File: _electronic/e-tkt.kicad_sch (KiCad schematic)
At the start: 1 part

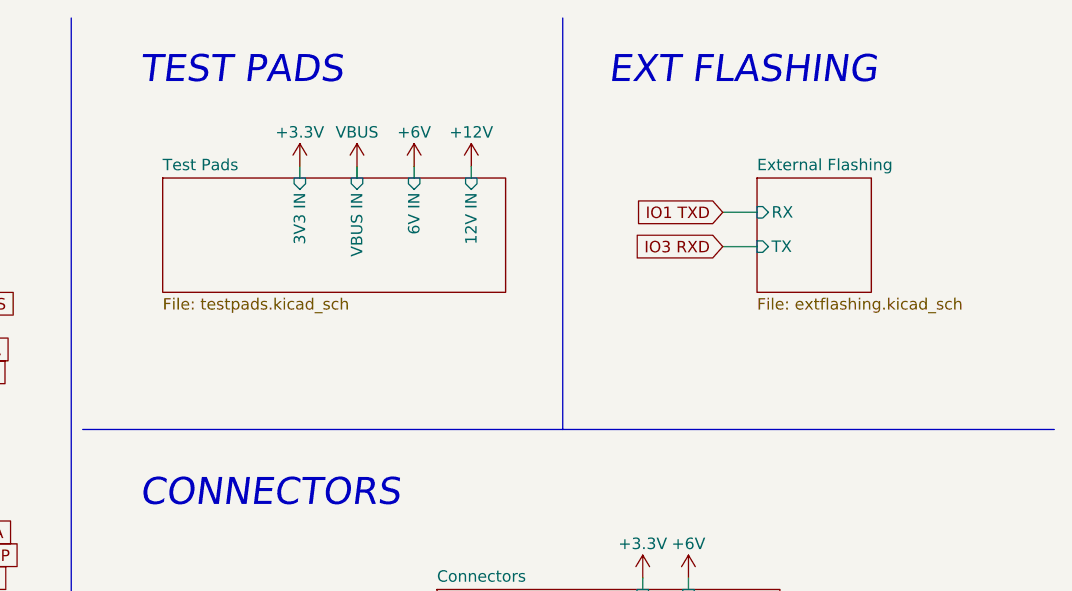
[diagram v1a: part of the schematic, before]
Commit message: revised pcb: direct power, leds, ftdi w/o 3v3
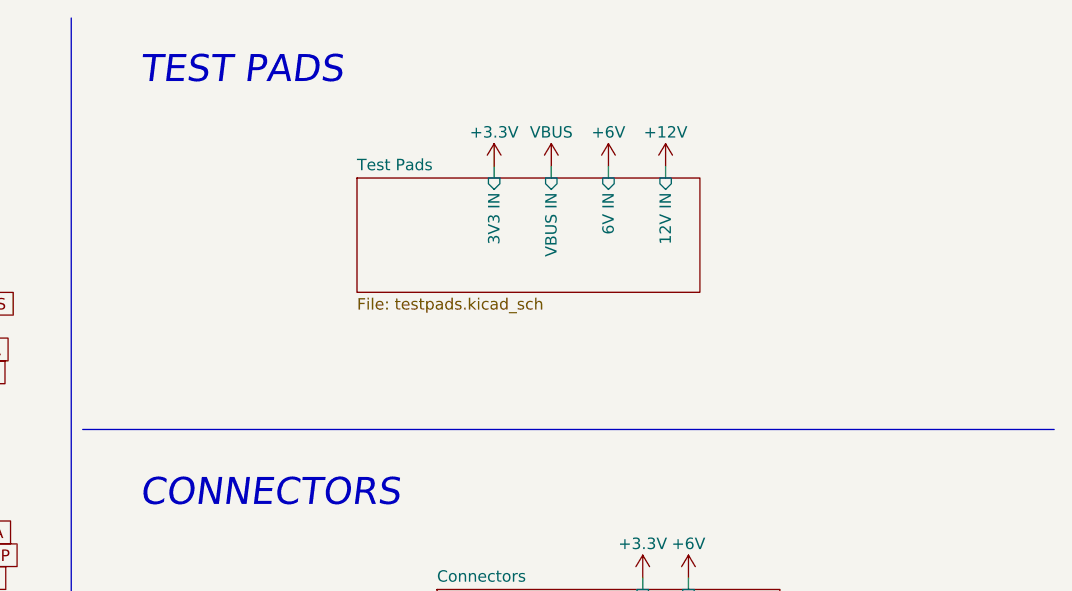
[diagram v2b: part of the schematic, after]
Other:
- removed sheet External Flashing
- note removed: "EXT FLASHING"

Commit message: v1 pcb
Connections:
- net MCU/IO27 BUZZER OUT renamed MCU/IO26 BUZZER OUT
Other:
- sheet Boot ports: added DFU OUT; removed RESET OUT
- sheet MCU ports: added IO26 BUZZER OUT; removed IO27 BUZZER OUT
- note added: "PADS"
- note removed: "TEST PADS"
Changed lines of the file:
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@@
     (stroke (width 0) (type default) (color 0 0 0 0))
   )
-  (text "TEST PADS" (at 184.15 20.32 0)
+  (text "PADS" (at 184.15 20.32 0)
     (effects (font (size 3 3) italic) (justify left bottom))
   )
@@
     )
   )
-  (global_label "IO0 RESET" (shape input) (at 67.31 109.22 0) (fields_autoplaced)
-    (effects (font (size 1.27 1.27)) (justify left))
-    (property "Intersheet References" "${INTERSHEET_REFS}" (id 0) (at 79.5807 109.1406 0)
+  (global_label "IO0 DFU" (shape input) (at 67.31 109.22 0) (fields_autoplaced)
+    (effects (font (size 1.27 1.27)) (justify left))
+    (property "Intersheet References" "${INTERSHEET_REFS}" (id 0) (at 77.5245 109.1406 0)
       (effects (font (size 1.27 1.27)) (justify left) hide)
     )
@@
     )
   )
-  (global_label "IO0 RESET" (shape input) (at 107.95 58.42 180) (fields_autoplaced)
-    (effects (font (size 1.27 1.27)) (justify right))
-    (property "Intersheet References" "${INTERSHEET_REFS}" (id 0) (at 95.6793 58.4994 0)
+  (global_label "IO0 DFU" (shape input) (at 107.95 58.42 180) (fields_autoplaced)
+    (effects (font (size 1.27 1.27)) (justify right))
+    (property "Intersheet References" "${INTERSHEET_REFS}" (id 0) (at 97.7355 58.3406 0)
       (effects (font (size 1.27 1.27)) (justify right) hide)
     )
@@
       (effects (font (size 1.27 1.27)) (justify left top))
     )
-    (pin "RESET OUT" input (at 63.5 109.22 0)
+    (pin "DFU OUT" input (at 63.5 109.22 0)
       (effects (font (size 1.27 1.27)) (justify right))
     )
@@
       (effects (font (size 1.27 1.27)) (justify right))
     )
-    (pin "IO27 BUZZER OUT" input (at 149.86 83.82 0)
+    (pin "IO26 BUZZER OUT" input (at 149.86 83.82 0)
       (effects (font (size 1.27 1.27)) (justify right))
     )
@@
       (reference "#PWR0128") (unit 1) (value "+6V") (footprint "")
     )
+    (path "/101993a2-8c13-4c99-b45a-f486b8a836ae/4741fdff-cf20-405c-8df9-b0efece63751"
+      (reference "#PWR0129") (unit 1) (value "GNDREF") (footprint "")
+    )
     (path "/101993a2-8c13-4c99-b45a-f486b8a836ae/b2ca76e4-3a79-40a6-bbdf-055e674ad637"
       (reference "#PWR0130") (unit 1) (value "GNDREF") (footprint "")
@@
       (reference "#PWR0188") (unit 1) (value "+12V") (footprint "")
     )
-    (path "/101993a2-8c13-4c99-b45a-f486b8a836ae/b900f311-a484-4187-a9ac-83ef2eca9cdf"
-      (reference "#PWR0194") (unit 1) (value "GNDREF") (footprint "")
-    )
     (path "/101993a2-8c13-4c99-b45a-f486b8a836ae/c73cd793-7bb6-49a6-8bf3-bf2dc45d0e58"
       (reference "A_NEMA1") (unit 1) (value "8+8 pin") (footprint "SnapEDA Library:Pololu_Breakout-16_15.2x20.3mm")
     )
+    (path "/53dc24b1-e06e-42b0-9cce-919318864537/c708e976-d434-4784-8384-a21eac2e20cc"
+      (reference "C_DFU1") (unit 1) (value "0.1uF 50V") (footprint "Capacitor_SMD:C_0603_1608Metric_Pad1.08x0.95mm_HandSolder")
+    )
     (path "/53dc24b1-e06e-42b0-9cce-919318864537/c161ff46-3126-42d4-ac2d-a86add82b65e"
       (reference "C_ENA1") (unit 1) (value "0.1uF 50V") (footprint "Capacitor_SMD:C_0603_1608Metric_Pad1.08x0.95mm_HandSolder")
@@
       (reference "C_POW_OUT5") (unit 1) (value "22uF 25V") (footprint "Capacitor_SMD:C_1210_3225Metric_Pad1.33x2.70mm_HandSolder")
     )
-    (path "/53dc24b1-e06e-42b0-9cce-919318864537/c708e976-d434-4784-8384-a21eac2e20cc"
-      (reference "C_RST1") (unit 1) (value "0.1uF 50V") (footprint "Capacitor_SMD:C_0603_1608Metric_Pad1.08x0.95mm_HandSolder")
-    )
     (path "/500f785f-7d37-4530-93ef-964340f250e0/29215e2e-bd3e-478f-8c8a-2609da7e48de"
       (reference "C_SER2") (unit 1) (value "47pF 5V") (footprint "Capacitor_SMD:C_0603_1608Metric_Pad1.08x0.95mm_HandSolder")
@@
       (reference "R_AUTO2") (unit 1) (value "10K (5%)") (footprint "Resistor_SMD:R_0603_1608Metric_Pad0.98x0.95mm_HandSolder")
     )
+    (path "/53dc24b1-e06e-42b0-9cce-919318864537/80289846-45bb-4f7e-8a56-6a469cee6e49"
+      (reference "R_DFU1") (unit 1) (value "10K (5%)") (footprint "Resistor_SMD:R_0603_1608Metric_Pad0.98x0.95mm_HandSolder")
+    )
     (path "/53dc24b1-e06e-42b0-9cce-919318864537/f9878306-6ebd-4529-86fc-8fe33906cf59"
       (reference "R_ENA1") (unit 1) (value "10K (5%)") (footprint "Resistor_SMD:R_0603_1608Metric_Pad0.98x0.95mm_HandSolder")
@@
       (reference "R_POW_FFB1") (unit 1) (value "11K") (footprint "Resistor_SMD:R_0603_1608Metric_Pad0.98x0.95mm_HandSolder")
     )
-    (path "/53dc24b1-e06e-42b0-9cce-919318864537/80289846-45bb-4f7e-8a56-6a469cee6e49"
-      (reference "R_RST1") (unit 1) (value "10K (5%)") (footprint "Resistor_SMD:R_0603_1608Metric_Pad0.98x0.95mm_HandSolder")
-    )
     (path "/500f785f-7d37-4530-93ef-964340f250e0/1d27ab48-a640-4f47-bc17-bdcd69db5732"
       (reference "R_RX1") (unit 1) (value "27R") (footprint "Resistor_SMD:R_0603_1608Metric_Pad0.98x0.95mm_HandSolder")
@@
       (reference "R_WIFI1") (unit 1) (value "10K(5%)") (footprint "Resistor_SMD:R_0603_1608Metric_Pad0.98x0.95mm_HandSolder")
     )
+    (path "/53dc24b1-e06e-42b0-9cce-919318864537/d348eb6c-e41c-436a-ae0e-698c5c035baa"
+      (reference "SW_DFU1") (unit 1) (value "B3FS-1000") (footprint "b3fs:B3FS-1000")
+    )
     (path "/53dc24b1-e06e-42b0-9cce-919318864537/a455153a-05f9-4e85-901e-8958d4f3b17b"
       (reference "SW_ENA1") (unit 1) (value "B3FS-1000") (footprint "b3fs:B3FS-1000")
     )
-    (path "/53dc24b1-e06e-42b0-9cce-919318864537/d348eb6c-e41c-436a-ae0e-698c5c035baa"
-      (reference "SW_RST1") (unit 1) (value "B3FS-1000") (footprint "b3fs:B3FS-1000")
-    )
     (path "/2d0c1513-867c-4f44-88ad-09ecf55e026a/29887617-5bc0-4b32-ac51-e4008f4b493b"
       (reference "SW_WIFI1") (unit 1) (value "B3FS-1000") (footprint "b3fs:B3FS-1000")
     )
-    (path "/80181399-56c9-4858-bcd2-be6de4dbffde/a2ae1716-c872-45b0-ada9-012773e72e0e"
-      (reference "TP_3.3v1") (unit 1) (value "TestPoint") (footprint "TestPoint:TestPoint_Pad_D1.0mm")
-    )
-    (path "/80181399-56c9-4858-bcd2-be6de4dbffde/7dfcde2e-43b0-42d7-8f37-7932f448318d"
-      (reference "TP_5v1") (unit 1) (value "TestPoint") (footprint "TestPoint:TestPoint_Pad_D1.0mm")
-    )
-    (path "/80181399-56c9-4858-bcd2-be6de4dbffde/0d1cefda-0da1-419e-8d72-b6b1e29406d4"
-      (reference "TP_6v1") (unit 1) (value "TestPoint") (footprint "TestPoint:TestPoint_Pad_D1.0mm")
-    )
-    (path "/80181399-56c9-4858-bcd2-be6de4dbffde/8cef06b1-cb55-4287-a2c1-e0e76cd67f80"
-      (reference "TP_12v1") (unit 1) (value "TestPoint") (footprint "TestPoint:TestPoint_Pad_D1.0mm")
-    )
-    (path "/80181399-56c9-4858-bcd2-be6de4dbffde/c13fc93a-0972-4a87-8f24-0804bf570334"
-      (reference "TP_GND3") (unit 1) (value "TestPoint") (footprint "TestPoint:TestPoint_Pad_D1.0mm")
-    )
     (path "/973f9b7f-d992-45f9-a125-51db85018136/fdecbef2-8cfc-4ede-8ea0-7a11182a7ade"

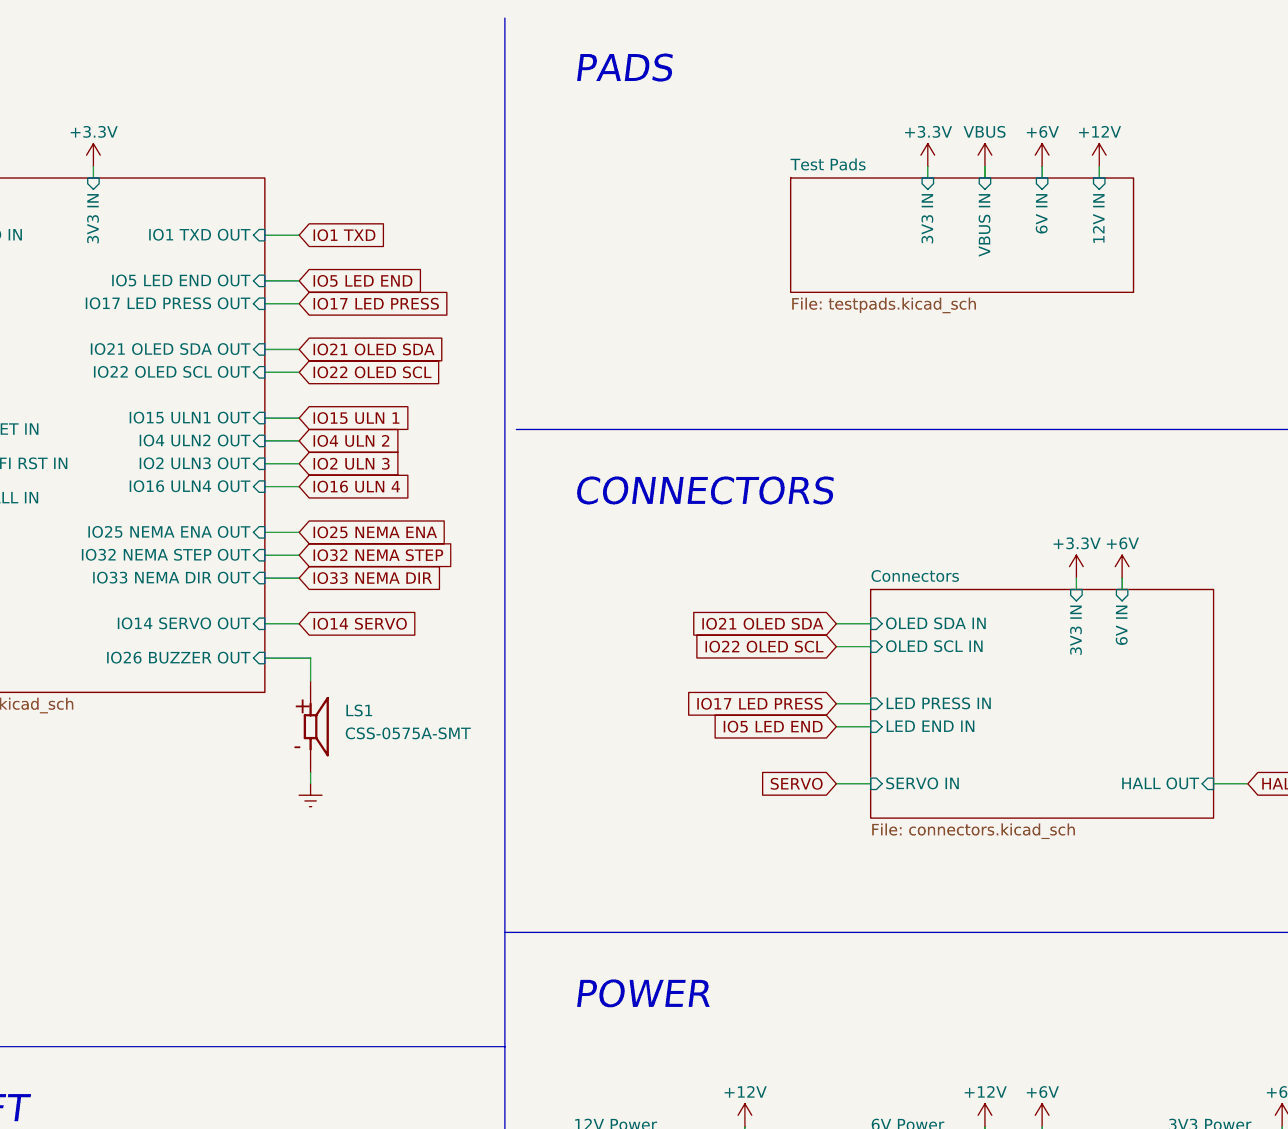
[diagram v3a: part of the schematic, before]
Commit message: led resistor revision, b.o.m. and pcb anotation
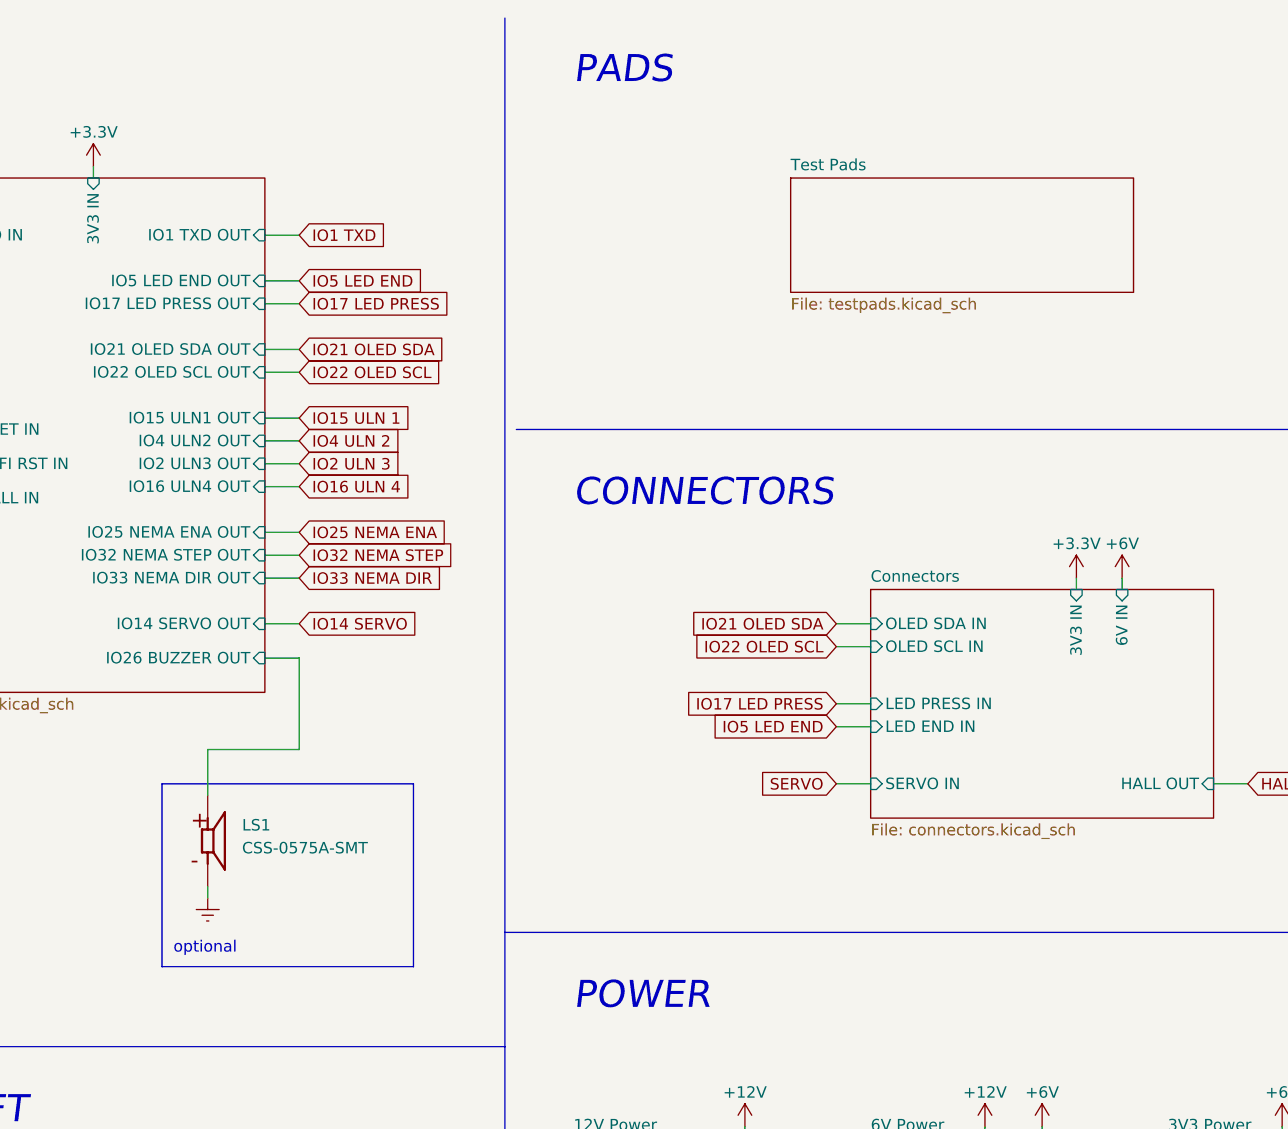
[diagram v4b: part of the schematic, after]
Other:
- sheet Test Pads ports: added none; removed 12V IN, 3V3 IN, 6V IN, VBUS IN
- note added: "optional"
- moved on the sheet: LS1

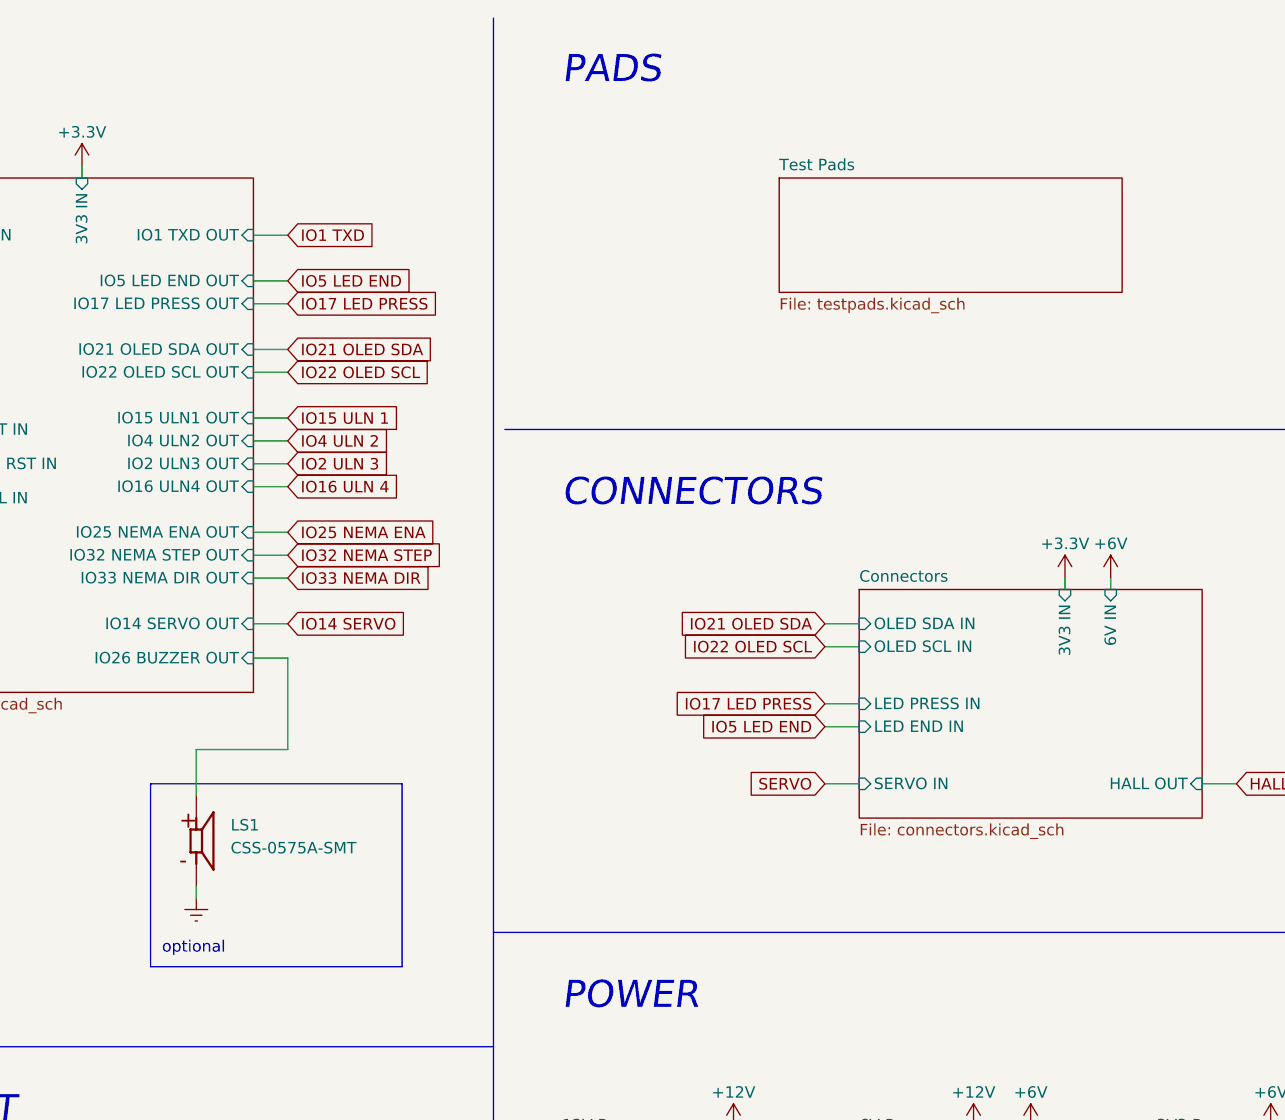
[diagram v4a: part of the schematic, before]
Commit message: schematics and pcb cleanup
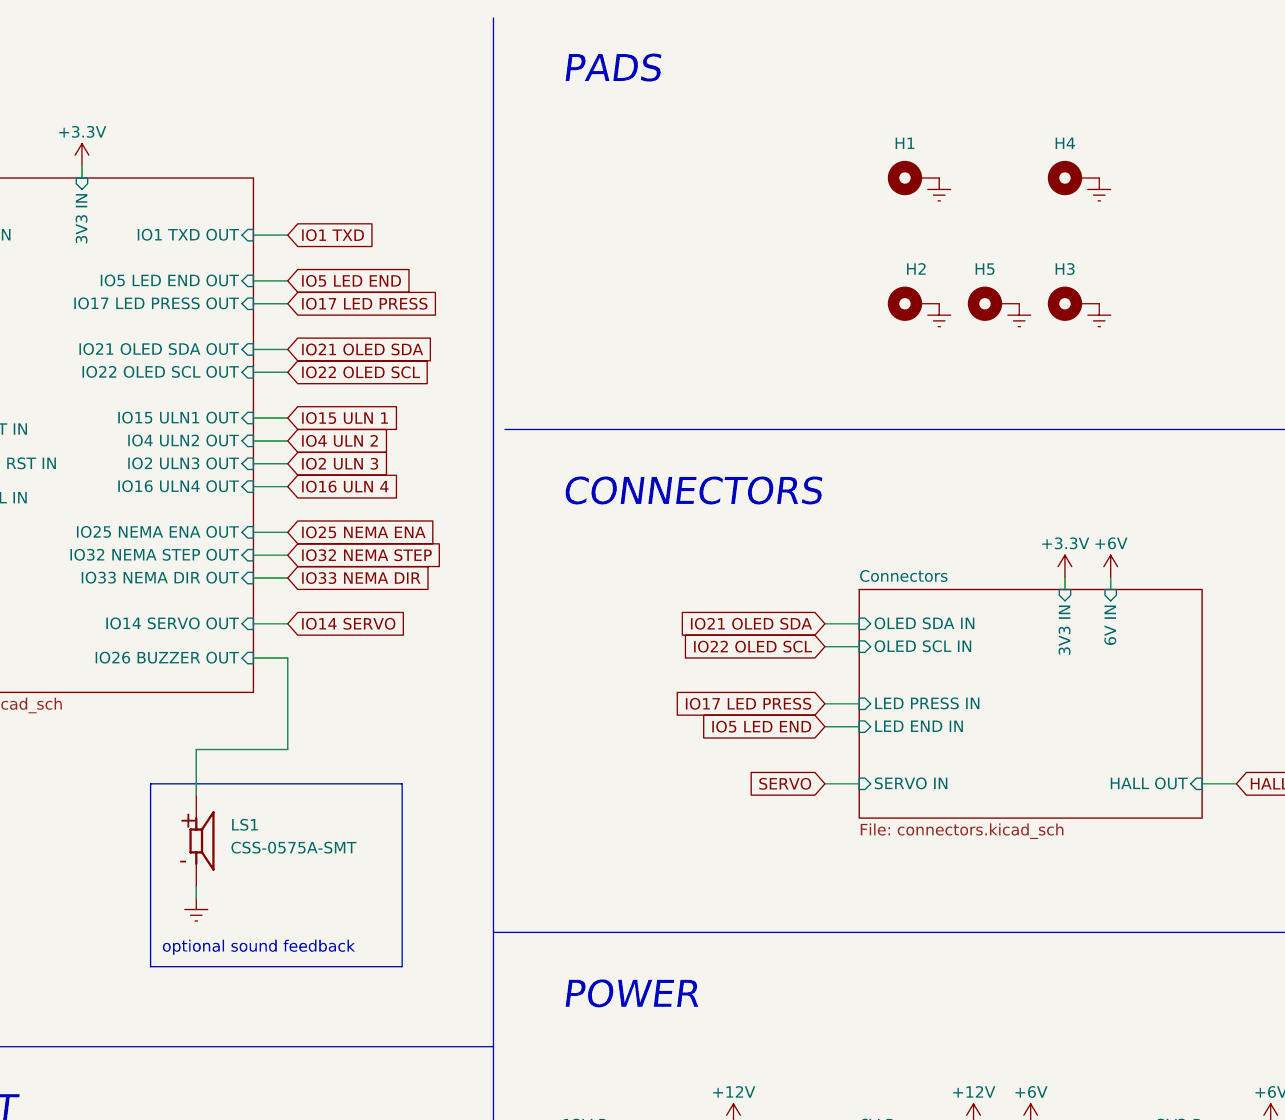
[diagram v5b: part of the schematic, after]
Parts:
- added H1, H2, H3, H4, H5: M3, MountingHole:MountingHole_3.2mm_M3_Pad_Via, symbol Mechanical:MountingHole_Pad
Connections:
- net GNDREF: now also H1.1, H2.1, H3.1, H4.1, H5.1
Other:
- removed sheet Test Pads
- note added: "optional sound feedback"
- note removed: "optional"
- title: E-TKT -> E-TKT v1.0
